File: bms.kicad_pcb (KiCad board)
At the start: 4 copper layers, 100 x 67 mm, 179 parts, among them J1 CELL_TAPS, J2 I2C_IN, J3 THERM_1, J4 THERM_2, J5 SWD, Q1 AO3400A, Q10 AO3400A, Q11 AO3400A, Q12 AO3400A, Q13 AO3400A, Q14 AO3400A, Q15 AO3400A, Q16 AO3400A, Q17 AO3400A, Q18 AO3400A, Q19 AO3400A, Q2 AO3400A, Q20 AO3400A, Q3 AO3400A, Q4 AO3400A, Q5 AO3400A, Q6 AO3400A, Q7 AO3400A, Q8 AO3400A, Q9 AO3400A, SW1 SW_Push, U1 LMR516xx, U2 STM32F103C8Tx, U3 ADuM1252, U4 MAX14920, U5 MAX11163, U6 MAX6126, Y1 8M

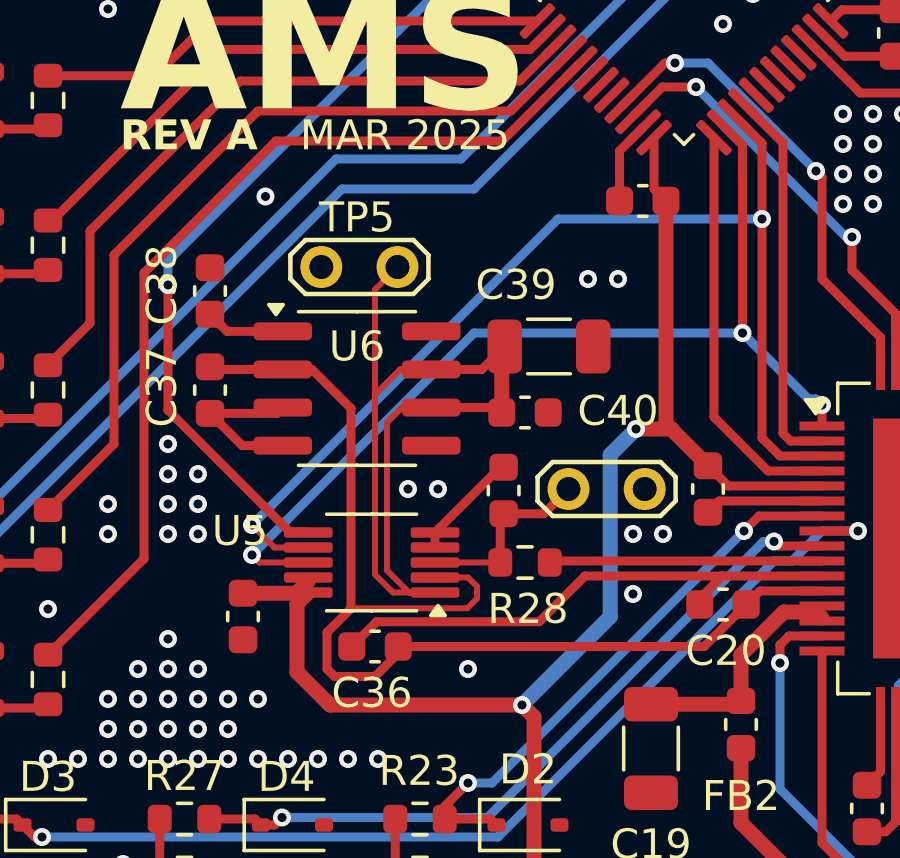
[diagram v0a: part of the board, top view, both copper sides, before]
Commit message: pcb: Add more GND vias near reference and ADC
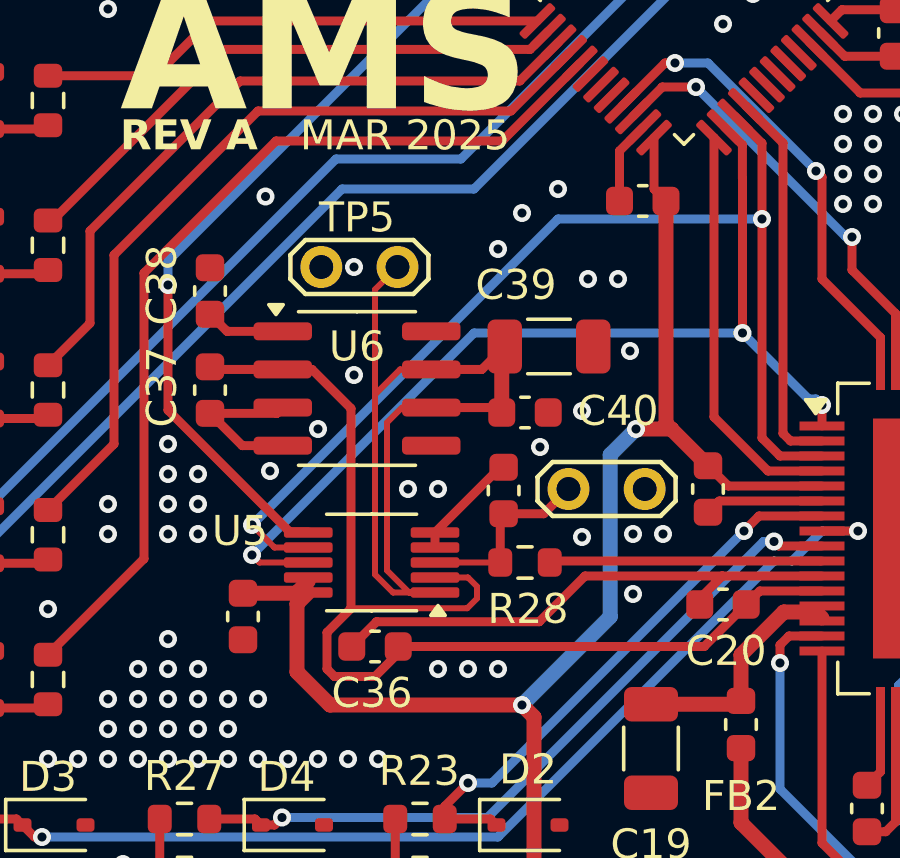
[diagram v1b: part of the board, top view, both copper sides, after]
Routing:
- net GND: vias 660 -> 673

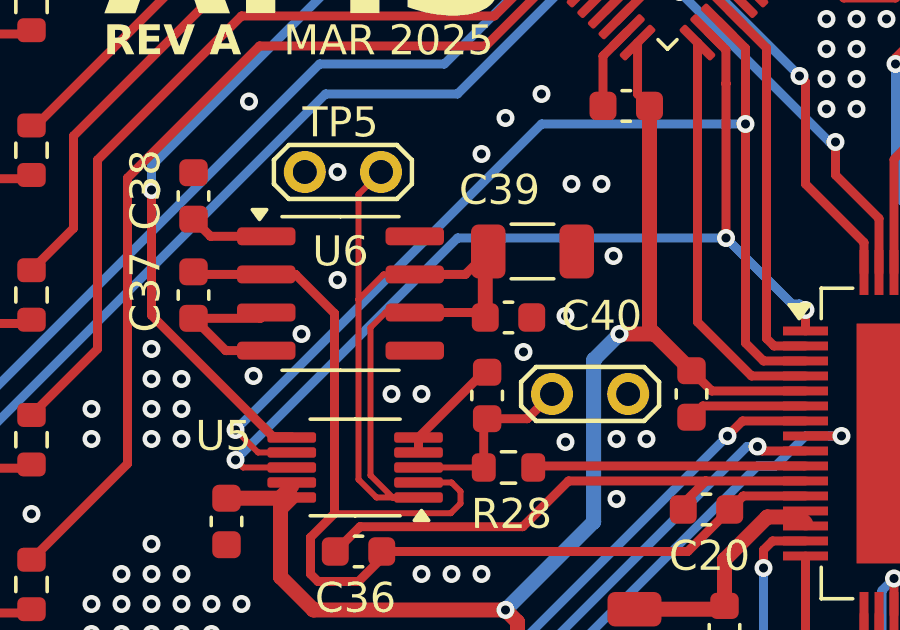
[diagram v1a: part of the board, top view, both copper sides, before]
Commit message: pcb: Remove extra reference OUTS trace
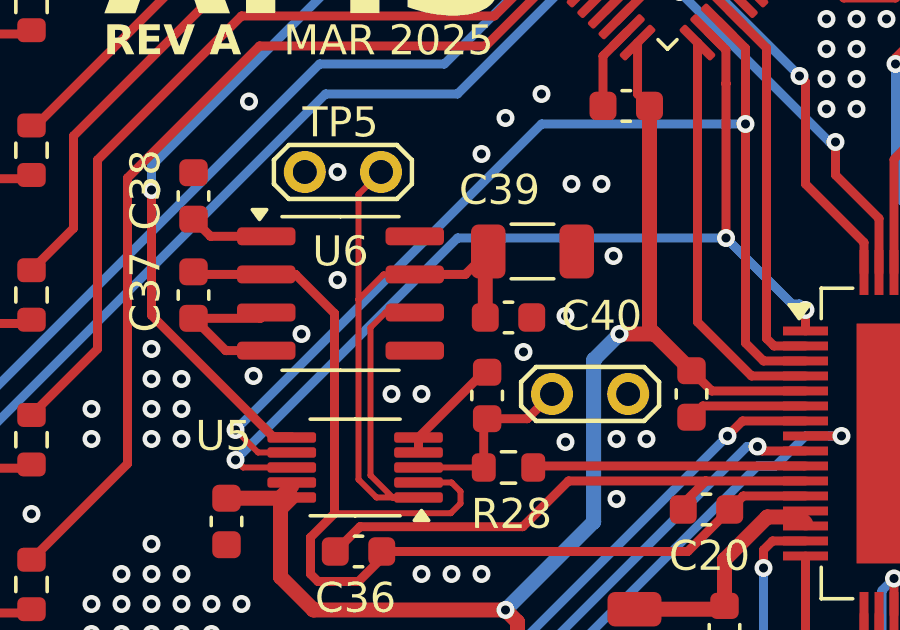
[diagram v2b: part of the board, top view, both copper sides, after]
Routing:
- net Net-(U5-REF): track 31.0 -> 28.6 mm
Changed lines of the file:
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@@
-	)
-	(segment
-		(start 77.775 83.285)
-		(end 79.96 83.285)
-		(width 0.3)
-		(layer "F.Cu")
-		(net 39)
 	)
 	(segment
@@
 		(layer "F.Cu")
 		(net 39)
-	)
-	(segment
-		(start 79.96 83.285)
-		(end 80.125 83.45)
-		(width 0.3)
-		(layer "F.Cu")
-		(net 39)

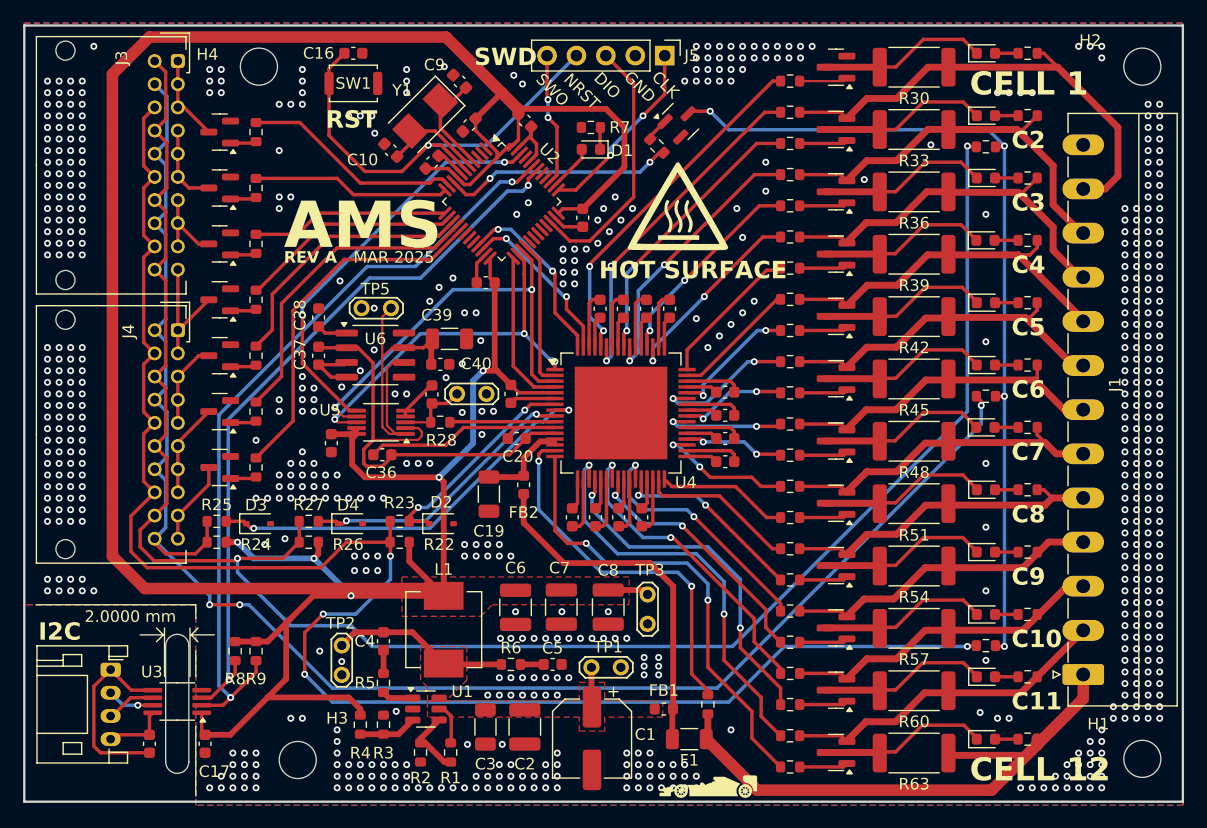
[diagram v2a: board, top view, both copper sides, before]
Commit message: pcb: Cleanup tracks
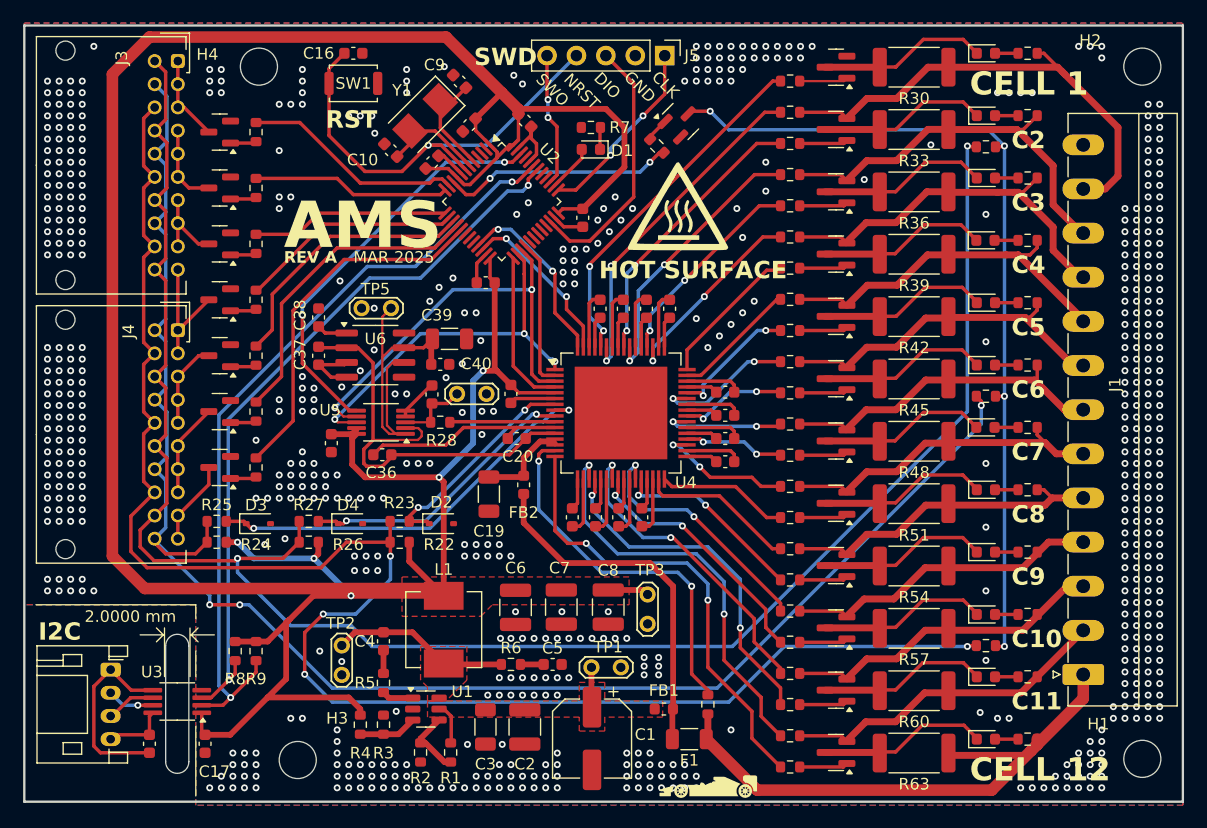
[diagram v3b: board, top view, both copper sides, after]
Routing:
- net TAP8: track 30.3 -> 28.4 mm
- net TAP11: track 29.4 -> 28.8 mm
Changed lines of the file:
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@@
 	)
 	(segment
-		(start 79.853856 66.746144)
-		(end 79.851992 66.748008)
-		(width 0.3)
-		(layer "F.Cu")
-		(net 6)
-	)
-	(segment
 		(start 85.7875 84.0125)
 		(end 85.6 83.825)
@@
 	)
 	(segment
-		(start 93.25 93.35)
-		(end 93.275 93.375)
-		(width 0.2)
-		(layer "F.Cu")
-		(net 15)
-	)
-	(segment
 		(start 95.25 97.1)
 		(end 94.925 97.425)
@@
 	)
 	(segment
-		(start 95.25 93.35)
-		(end 95.275 93.375)
-		(width 0.2)
-		(layer "F.Cu")
-		(net 16)
-	)
-	(segment
 		(start 94.925 97.425)
 		(end 94.3 97.425)
@@
 	)
 	(segment
-		(start 97.25 93.35)
-		(end 97.274999 93.374999)
-		(width 0.2)
-		(layer "F.Cu")
-		(net 18)
-	)
-	(segment
 		(start 96.75 95.424999)
 		(end 96.299999 95.875)
@@
 	)
 	(segment
-		(start 99.25 93.35)
-		(end 99.275 93.375)
-		(width 0.2)
-		(layer "F.Cu")
-		(net 20)
-	)
-	(segment
 		(start 98.75 95.425)
 		(end 98.75 93.35)
@@
 	)
 	(segment
-		(start 102.2 90.9)
-		(end 102.225 90.875)
-		(width 0.2)
-		(layer "F.Cu")
-		(net 23)
-	)
-	(segment
 		(start 104.275 89.4)
 		(end 102.2 89.4)
@@
 	)
 	(segment
-		(start 102.2 88.9)
-		(end 102.225 88.875)
-		(width 0.2)
-		(layer "F.Cu")
-		(net 25)
-	)
-	(segment
 		(start 106.275 89.225)
 		(end 106.275 89.85)
@@
 	)
 	(segment
-		(start 102.2 86.9)
-		(end 102.225 86.875)
-		(width 0.2)
-		(layer "F.Cu")
-		(net 27)
-	)
-	(segment
 		(start 105.95 86.9)
 		(end 106.275 87.225)
@@
 	)
 	(segment
-		(start 102.2 84.9)
-		(end 102.225 84.875)
-		(width 0.2)
-		(layer "F.Cu")
-		(net 29)
-	)
-	(segment
 		(start 106.275 85.225)
 		(end 106.275 85.85)
@@
 	)
 	(segment
-		(start 99.75 81.95)
-		(end 99.725 81.925)
-		(width 0.2)
-		(layer "F.Cu")
-		(net 30)
-	)
-	(segment
 		(start 99.75 78.175)
 		(end 100.075 77.85)
@@
 	)
 	(segment
-		(start 97.75 81.95)
-		(end 97.725 81.925)
-		(width 0.2)
-		(layer "F.Cu")
-		(net 33)
-	)
-	(segment
 		(start 96.25 79.875)
 		(end 96.7 79.425)
@@
 	(segment
 		(start 95.75 81.95)
-		(end 95.725 81.925)
-		(width 0.2)
-		(layer "F.Cu")
-		(net 35)
-	)
-	(segment
-		(start 95.75 81.95)
 		(end 95.75 78.2)
 		(width 0.3)
@@
 	)
 	(segment
-		(start 135.84 106)
-		(end 136.25 106.41)
-		(width 0.5)
-		(layer "F.Cu")
-		(net 72)
-	)
-	(segment
 		(start 136.25 106.581836)
 		(end 131.031836 111.8)
@@
 	)
 	(segment
-		(start 136.24 106.4)
-		(end 136.25 106.41)
-		(width 0.3)
-		(layer "F.Cu")
-		(net 72)
-	)
-	(segment
 		(start 117.632954 114.3)
 		(end 120.205682 114.3)
@@
 	)
 	(segment
-		(start 135.692726 94.272726)
-		(end 136.4 94.98)
-		(width 0.3)
-		(layer "F.Cu")
-		(net 80)
-	)
-	(segment
 		(start 115.9875 99.845454)
 		(end 117.714772 98.118182)
@@
 	)
 	(segment
-		(start 136.25 94.98)
-		(end 135.63 95.6)
-		(width 0.6)
-		(layer "F.Cu")
-		(net 80)
-	)
-	(segment
 		(start 136.4 94.98)
 		(end 133.72 94.98)
@@
 	)
 	(segment
-		(start 127.175 86.199999)
-		(end 127.175 86.325)
-		(width 0.3)
-		(layer "F.Cu")
-		(net 88)
-	)
-	(segment
 		(start 127.6 87)
 		(end 127.6 86.624999)
@@
 	)
 	(segment
-		(start 90.75 88.45)
-		(end 90.8 88.4)
-		(width 0.2)
-		(layer "F.Cu")
-		(net 138)
-	)
-	(segment
 		(start 90.8 88.4)
 		(end 81.775 88.4)
@@
 	)
 	(segment
-		(start 102.2 83.9)
-		(end 102.45 83.9)
-		(width 0.3)
-		(layer "F.Cu")
-		(net 142)
-	)
-	(segment
 		(start 109.075 75.325)
 		(end 110.275 75.325)
@@
 	)
 	(segment
-		(start 97.2 99.2)
-		(end 96.8 98.8)
-		(width 0.3)
-		(layer "B.Cu")
-		(net 149)
-	)
-	(segment
-		(start 96.8 98.8)
-		(end 94 96)
+		(start 94 96)
+		(end 97.2 99.2)
 		(width 0.3)
 		(layer "B.Cu")
